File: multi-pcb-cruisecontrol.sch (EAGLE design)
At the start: 28 parts, among them IC1 LM358N, K1 351, T1 BC618, X1 2.52B-ZR, X2 2.52B-ZR, X4 6B-ZR, X5 2.52B-ZR

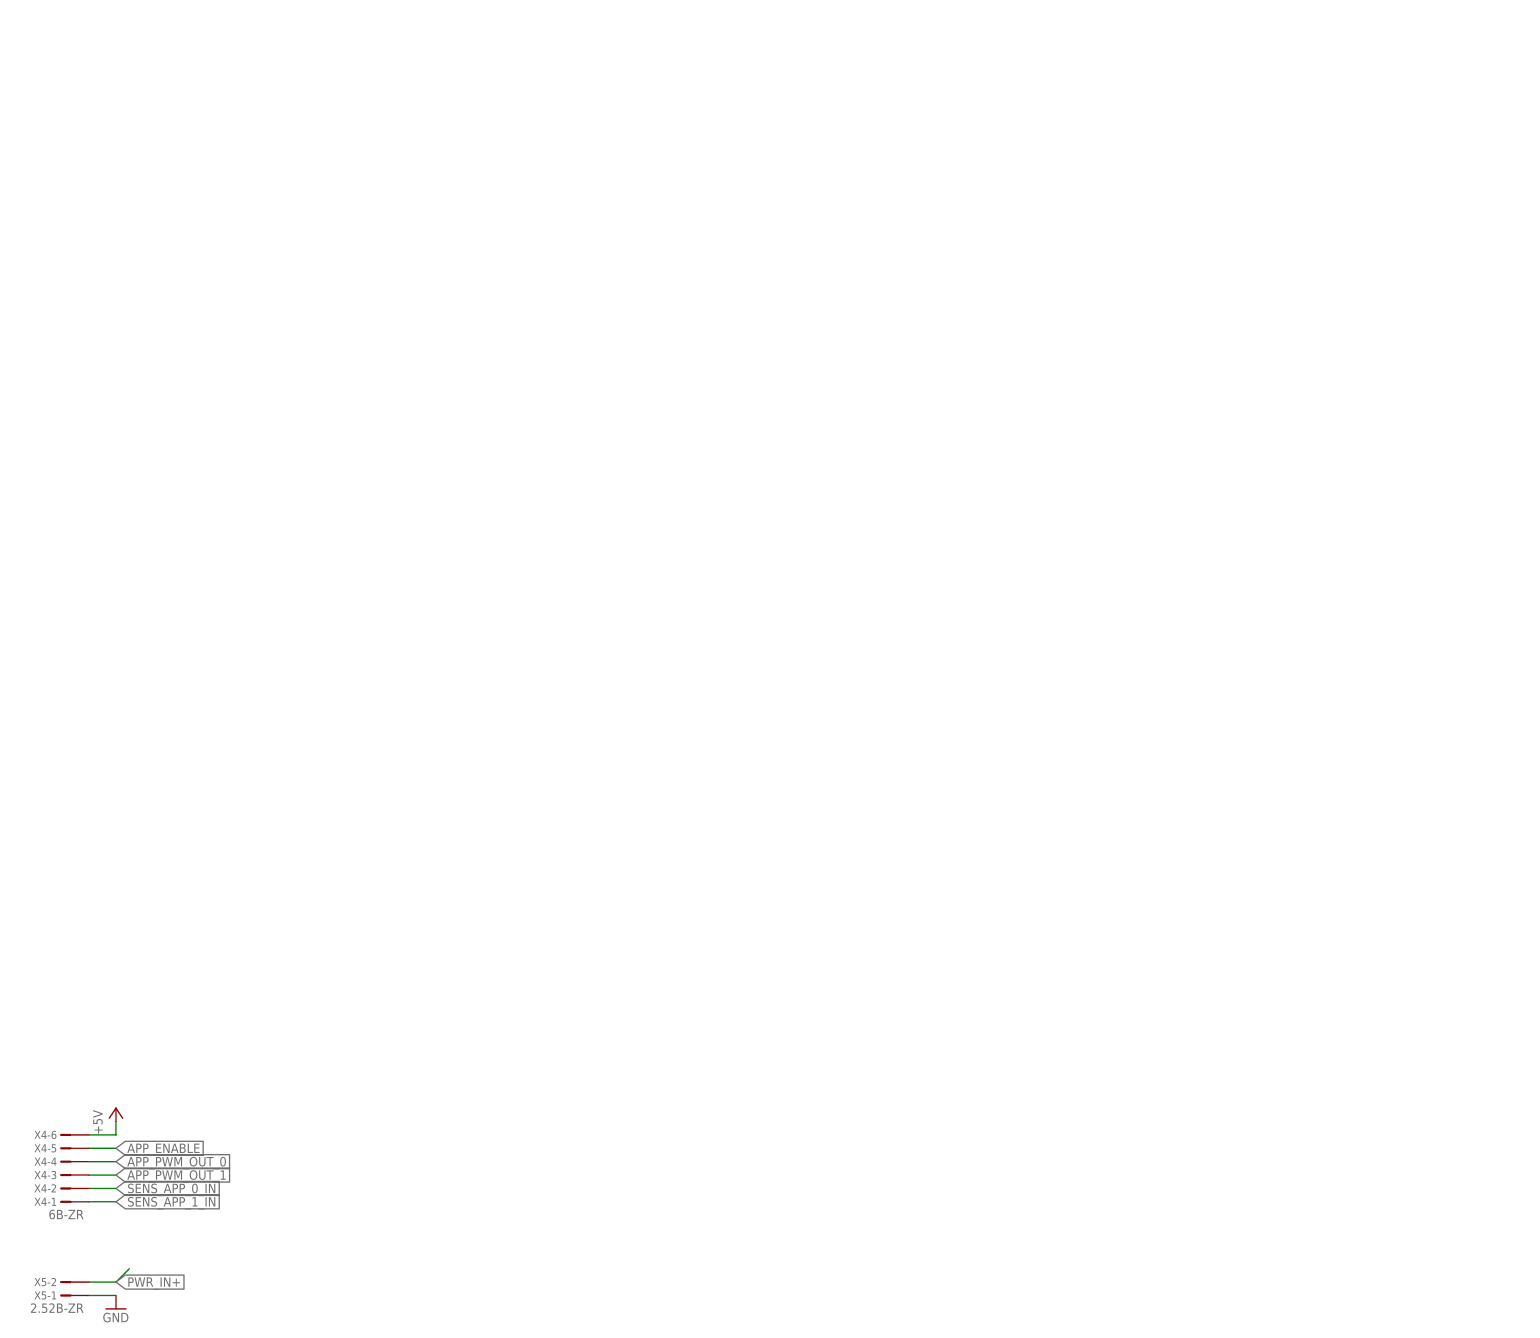
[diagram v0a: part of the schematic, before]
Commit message: Made schematic more compact/clean
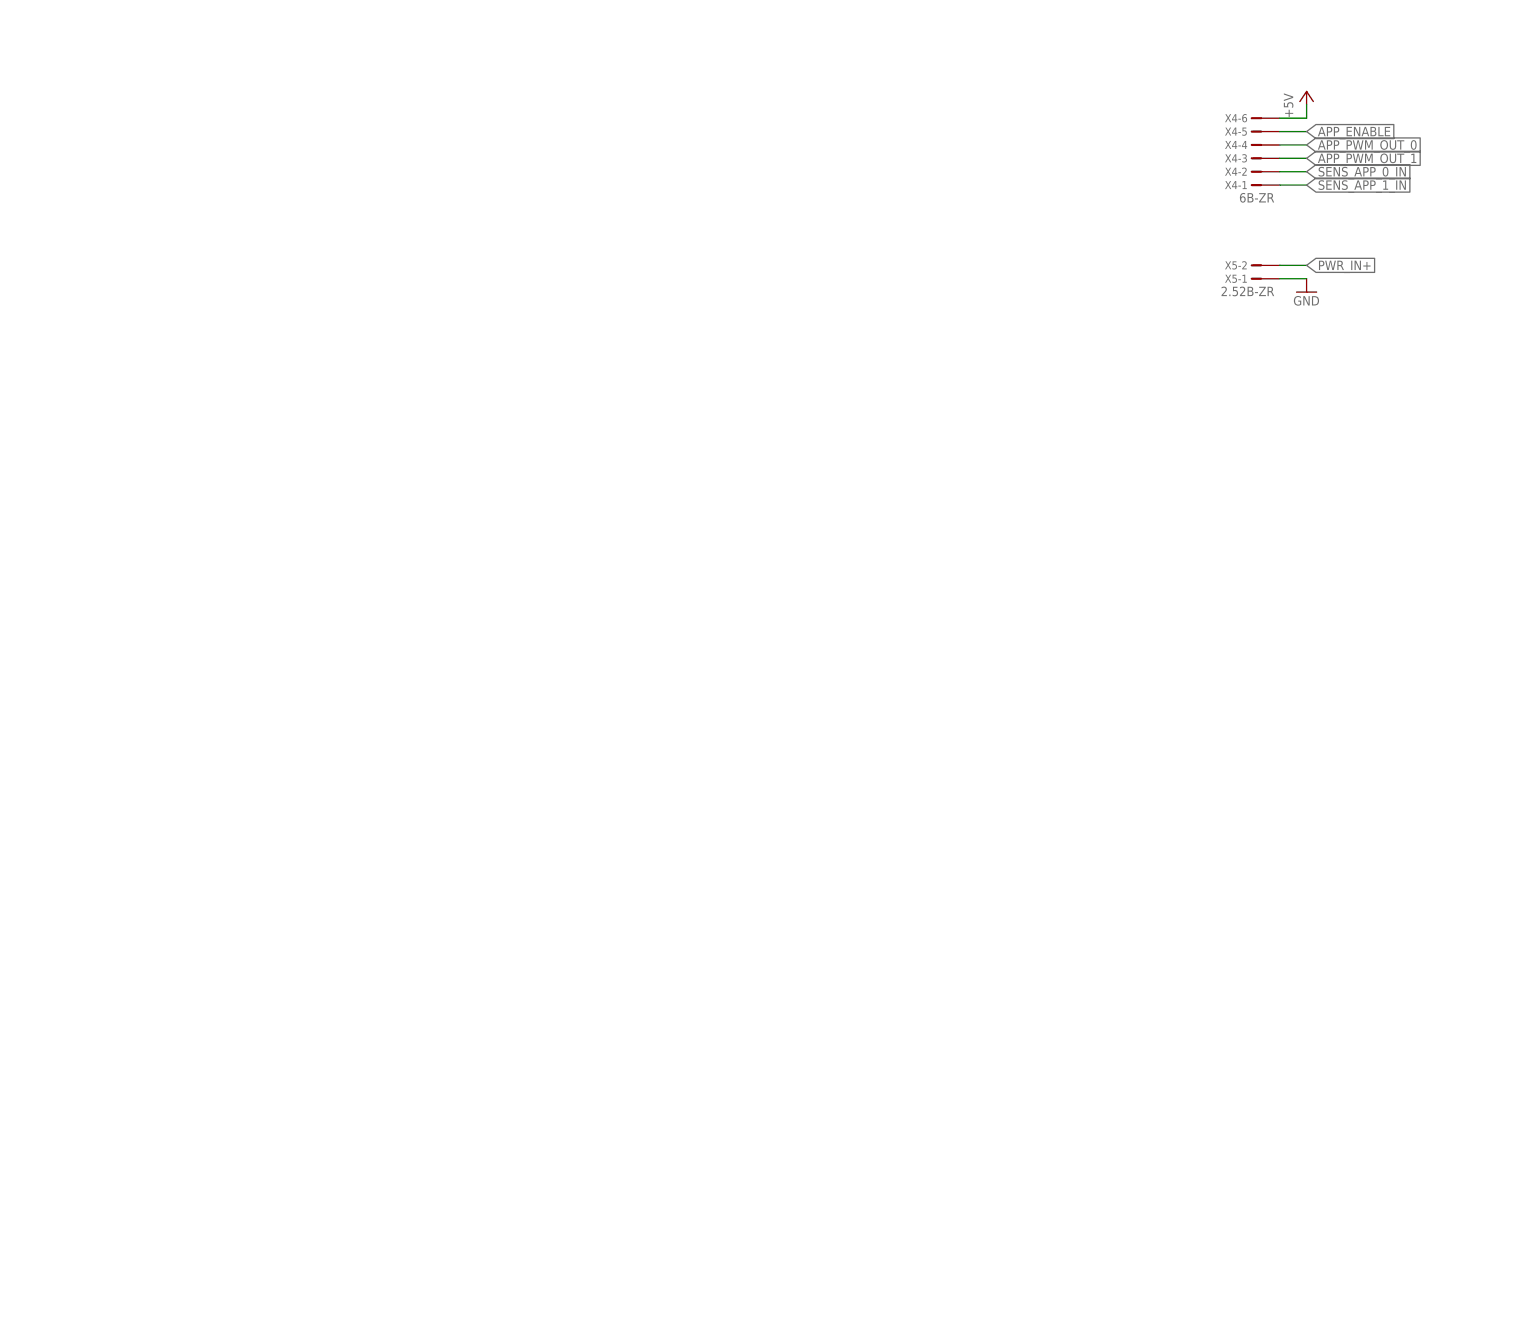
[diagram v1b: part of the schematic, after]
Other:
- moved on the sheet: X4-1, X4-2, X4-3, X4-4, X4-5, X4-6, X5-1, X5-2
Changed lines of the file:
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@@
 <attribute name="NAME" x="131.064" y="103.378" size="1.524" layer="95" rot="MR0"/>
 </instance>
-<instance part="X4" gate="-1" x="-157.48" y="-40.64" smashed="yes" rot="R180">
-<attribute name="NAME" x="-158.496" y="-39.878" size="1.524" layer="95" rot="R180"/>
-<attribute name="VALUE" x="-153.416" y="-42.164" size="1.778" layer="96" rot="R180"/>
-</instance>
-<instance part="X4" gate="-2" x="-157.48" y="-38.1" smashed="yes" rot="R180">
-<attribute name="NAME" x="-158.496" y="-37.338" size="1.524" layer="95" rot="R180"/>
-</instance>
-<instance part="X4" gate="-3" x="-157.48" y="-35.56" smashed="yes" rot="R180">
-<attribute name="NAME" x="-158.496" y="-34.798" size="1.524" layer="95" rot="R180"/>
-</instance>
-<instance part="X4" gate="-4" x="-157.48" y="-33.02" smashed="yes" rot="R180">
-<attribute name="NAME" x="-158.496" y="-32.258" size="1.524" layer="95" rot="R180"/>
-</instance>
-<instance part="X4" gate="-5" x="-157.48" y="-30.48" smashed="yes" rot="R180">
-<attribute name="NAME" x="-158.496" y="-29.718" size="1.524" layer="95" rot="R180"/>
-</instance>
-<instance part="X4" gate="-6" x="-157.48" y="-27.94" smashed="yes" rot="R180">
-<attribute name="NAME" x="-158.496" y="-27.178" size="1.524" layer="95" rot="R180"/>
-</instance>
-<instance part="X5" gate="-1" x="-157.48" y="-58.42" smashed="yes" rot="R180">
-<attribute name="NAME" x="-158.496" y="-57.658" size="1.524" layer="95" rot="R180"/>
-<attribute name="VALUE" x="-153.416" y="-59.944" size="1.778" layer="96" rot="R180"/>
-</instance>
-<instance part="X5" gate="-2" x="-157.48" y="-55.88" smashed="yes" rot="R180">
-<attribute name="NAME" x="-158.496" y="-55.118" size="1.524" layer="95" rot="R180"/>
-</instance>
-<instance part="GND1" gate="1" x="-147.32" y="-60.96" smashed="yes">
-<attribute name="VALUE" x="-149.86" y="-63.5" size="1.778" layer="96"/>
-</instance>
-<instance part="P+1" gate="1" x="-147.32" y="-22.86" smashed="yes">
-<attribute name="VALUE" x="-149.86" y="-27.94" size="1.778" layer="96" rot="R90"/>
+<instance part="X4" gate="-1" x="68.58" y="152.4" smashed="yes" rot="R180">
+<attribute name="NAME" x="67.564" y="153.162" size="1.524" layer="95" rot="R180"/>
+<attribute name="VALUE" x="72.644" y="150.876" size="1.778" layer="96" rot="R180"/>
+</instance>
+<instance part="X4" gate="-2" x="68.58" y="154.94" smashed="yes" rot="R180">
+<attribute name="NAME" x="67.564" y="155.702" size="1.524" layer="95" rot="R180"/>
+</instance>
+<instance part="X4" gate="-3" x="68.58" y="157.48" smashed="yes" rot="R180">
+<attribute name="NAME" x="67.564" y="158.242" size="1.524" layer="95" rot="R180"/>
+</instance>
+<instance part="X4" gate="-4" x="68.58" y="160.02" smashed="yes" rot="R180">
+<attribute name="NAME" x="67.564" y="160.782" size="1.524" layer="95" rot="R180"/>
+</instance>
+<instance part="X4" gate="-5" x="68.58" y="162.56" smashed="yes" rot="R180">
+<attribute name="NAME" x="67.564" y="163.322" size="1.524" layer="95" rot="R180"/>
+</instance>
+<instance part="X4" gate="-6" x="68.58" y="165.1" smashed="yes" rot="R180">
+<attribute name="NAME" x="67.564" y="165.862" size="1.524" layer="95" rot="R180"/>
+</instance>
+<instance part="X5" gate="-1" x="68.58" y="134.62" smashed="yes" rot="R180">
+<attribute name="NAME" x="67.564" y="135.382" size="1.524" layer="95" rot="R180"/>
+<attribute name="VALUE" x="72.644" y="133.096" size="1.778" layer="96" rot="R180"/>
+</instance>
+<instance part="X5" gate="-2" x="68.58" y="137.16" smashed="yes" rot="R180">
+<attribute name="NAME" x="67.564" y="137.922" size="1.524" layer="95" rot="R180"/>
+</instance>
+<instance part="GND1" gate="1" x="78.74" y="132.08" smashed="yes">
+<attribute name="VALUE" x="76.2" y="129.54" size="1.778" layer="96"/>
+</instance>
+<instance part="P+1" gate="1" x="78.74" y="170.18" smashed="yes">
+<attribute name="VALUE" x="76.2" y="165.1" size="1.778" layer="96" rot="R90"/>
 </instance>
 </instances>
@@
 <segment>
 <pinref part="X4" gate="-2" pin="1"/>
-<wire x1="-152.4" y1="-38.1" x2="-147.32" y2="-38.1" width="0.1524" layer="91"/>
-<label x="-147.32" y="-38.1" size="1.778" layer="95" xref="yes"/>
+<wire x1="73.66" y1="154.94" x2="78.74" y2="154.94" width="0.1524" layer="91"/>
+<label x="78.74" y="154.94" size="1.778" layer="95" xref="yes"/>
 </segment>
 </net>
@@
 <segment>
 <pinref part="X4" gate="-1" pin="1"/>
-<wire x1="-152.4" y1="-40.64" x2="-147.32" y2="-40.64" width="0.1524" layer="91"/>
-<label x="-147.32" y="-40.64" size="1.778" layer="95" xref="yes"/>
+<wire x1="73.66" y1="152.4" x2="78.74" y2="152.4" width="0.1524" layer="91"/>
+<label x="78.74" y="152.4" size="1.778" layer="95" xref="yes"/>
 </segment>
 </net>
@@
 <segment>
 <pinref part="X4" gate="-4" pin="1"/>
-<wire x1="-152.4" y1="-33.02" x2="-147.32" y2="-33.02" width="0.1524" layer="91"/>
-<label x="-147.32" y="-33.02" size="1.778" layer="95" xref="yes"/>
+<wire x1="73.66" y1="160.02" x2="78.74" y2="160.02" width="0.1524" layer="91"/>
+<label x="78.74" y="160.02" size="1.778" layer="95" xref="yes"/>
 </segment>
 </net>
@@
 <segment>
 <pinref part="X4" gate="-3" pin="1"/>
-<wire x1="-152.4" y1="-35.56" x2="-147.32" y2="-35.56" width="0.1524" layer="91"/>
-<label x="-147.32" y="-35.56" size="1.778" layer="95" xref="yes"/>
+<wire x1="73.66" y1="157.48" x2="78.74" y2="157.48" width="0.1524" layer="91"/>
+<label x="78.74" y="157.48" size="1.778" layer="95" xref="yes"/>
 </segment>
 </net>
@@
 <segment>
 <pinref part="X4" gate="-5" pin="1"/>
-<wire x1="-152.4" y1="-30.48" x2="-147.32" y2="-30.48" width="0.1524" layer="91"/>
-<label x="-147.32" y="-30.48" size="1.778" layer="95" xref="yes"/>
+<wire x1="73.66" y1="162.56" x2="78.74" y2="162.56" width="0.1524" layer="91"/>
+<label x="78.74" y="162.56" size="1.778" layer="95" xref="yes"/>
 </segment>
 </net>
@@
 <pinref part="X5" gate="-1" pin="1"/>
 <pinref part="GND1" gate="1" pin="GND"/>
-<wire x1="-152.4" y1="-58.42" x2="-147.32" y2="-58.42" width="0.1524" layer="91"/>
+<wire x1="73.66" y1="134.62" x2="78.74" y2="134.62" width="0.1524" layer="91"/>
 </segment>
 </net>
@@
 <segment>
 <pinref part="X4" gate="-6" pin="1"/>
-<wire x1="-152.4" y1="-27.94" x2="-147.32" y2="-27.94" width="0.1524" layer="91"/>
+<wire x1="73.66" y1="165.1" x2="78.74" y2="165.1" width="0.1524" layer="91"/>
 <pinref part="P+1" gate="1" pin="+5V"/>
-<wire x1="-147.32" y1="-27.94" x2="-147.32" y2="-25.4" width="0.1524" layer="91"/>
+<wire x1="78.74" y1="165.1" x2="78.74" y2="167.64" width="0.1524" layer="91"/>
 </segment>
 </net>
@@
 </segment>
 <segment>
-<label x="-147.32" y="-55.88" size="1.778" layer="95" xref="yes"/>
-<wire x1="-147.32" y1="-55.88" x2="-144.78" y2="-53.34" width="0.1524" layer="91"/>
+<label x="78.74" y="137.16" size="1.778" layer="95" xref="yes"/>
 <pinref part="X5" gate="-2" pin="1"/>
-<wire x1="-152.4" y1="-55.88" x2="-147.32" y2="-55.88" width="0.1524" layer="91"/>
-</segment>
-</net>
+<wire x1="73.66" y1="137.16" x2="78.74" y2="137.16" width="0.1524" layer="91"/>
+</segment>
+</net>

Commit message: updated some PCB's
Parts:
- R10, R11, R8, R9: value 10k -> 220k
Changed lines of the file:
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@@
 <part name="GND4" library="supply1" library_urn="urn:adsk.eagle:library:371" deviceset="GND" device=""/>
 <part name="P+4" library="supply1" library_urn="urn:adsk.eagle:library:371" deviceset="+5V" device=""/>
-<part name="R8" library="rcl" library_urn="urn:adsk.eagle:library:334" deviceset="R-EU_" device="0207/7" package3d_urn="urn:adsk.eagle:package:23493/2" value="10k"/>
-<part name="R9" library="rcl" library_urn="urn:adsk.eagle:library:334" deviceset="R-EU_" device="0207/7" package3d_urn="urn:adsk.eagle:package:23493/2" value="10k"/>
+<part name="R8" library="rcl" library_urn="urn:adsk.eagle:library:334" deviceset="R-EU_" device="0207/7" package3d_urn="urn:adsk.eagle:package:23493/2" value="220k"/>
+<part name="R9" library="rcl" library_urn="urn:adsk.eagle:library:334" deviceset="R-EU_" device="0207/7" package3d_urn="urn:adsk.eagle:package:23493/2" value="220k"/>
 <part name="GND25" library="supply1" library_urn="urn:adsk.eagle:library:371" deviceset="GND" device=""/>
-<part name="R10" library="rcl" library_urn="urn:adsk.eagle:library:334" deviceset="R-EU_" device="0207/7" package3d_urn="urn:adsk.eagle:package:23493/2" value="10k"/>
-<part name="R11" library="rcl" library_urn="urn:adsk.eagle:library:334" deviceset="R-EU_" device="0207/7" package3d_urn="urn:adsk.eagle:package:23493/2" value="10k"/>
+<part name="R10" library="rcl" library_urn="urn:adsk.eagle:library:334" deviceset="R-EU_" device="0207/7" package3d_urn="urn:adsk.eagle:package:23493/2" value="220k"/>
+<part name="R11" library="rcl" library_urn="urn:adsk.eagle:library:334" deviceset="R-EU_" device="0207/7" package3d_urn="urn:adsk.eagle:package:23493/2" value="220k"/>
 <part name="GND26" library="supply1" library_urn="urn:adsk.eagle:library:371" deviceset="GND" device=""/>
 <part name="IC1" library="linear" library_urn="urn:adsk.eagle:library:262" deviceset="LM358" device="N" package3d_urn="urn:adsk.eagle:package:16409/2"/>
